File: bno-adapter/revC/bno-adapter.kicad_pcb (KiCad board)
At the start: 2 copper layers, 50.8 x 38.1 mm, 15 parts, among them P1 Mezzanine-Header, P2 CONN_01X04, P3 CONN_01X06, P4 Spacer, P5 Spacer, P6 Spacer, P7 Spacer

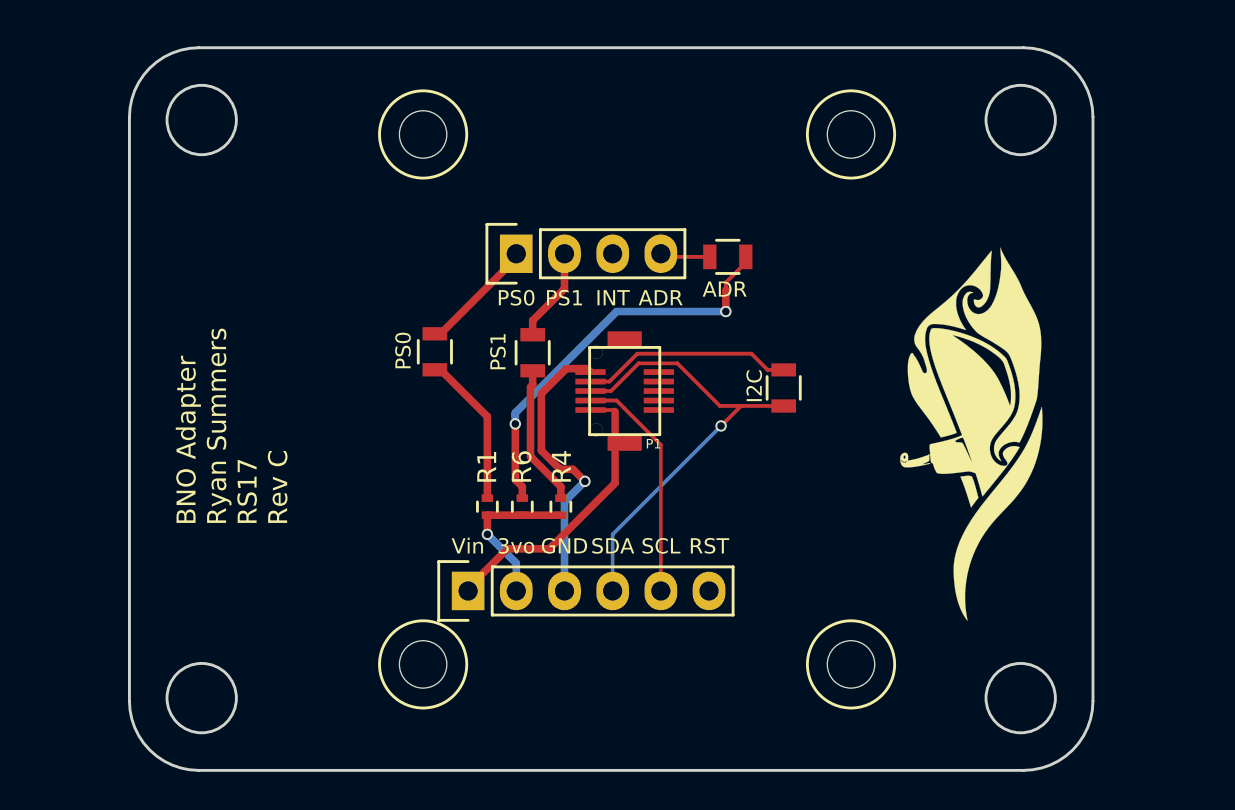
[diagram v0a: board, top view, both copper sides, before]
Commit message: Addition of VRML v2 model files and finished BNO adapter
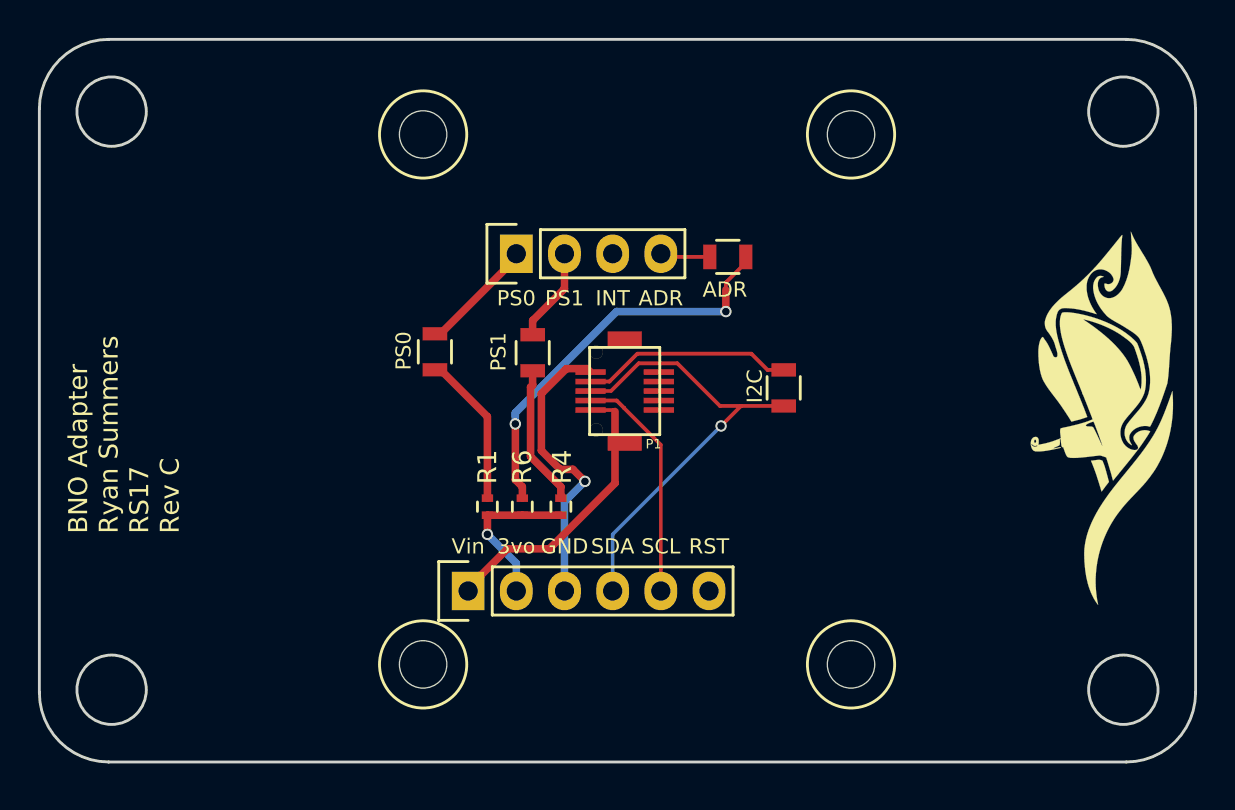
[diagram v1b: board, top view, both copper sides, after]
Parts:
- moved G*** 6.93 mm to (155.4, 101.4)
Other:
- board size 50.8 x 38.1 mm -> 61 x 38.1 mm
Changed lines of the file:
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@@
 (kicad_pcb (version 4) (host pcbnew 4.0.5-e0-6337~49~ubuntu16.04.1)
   (general
-    (links 0)
+    (links 15)
     (no_connects 0)
-    (area 103.785599 81.901203 154.735601 120.151205)
+    (area 99.035799 81.458999 160.145801 119.709001)
     (thickness 1.6)
     (drawings 35)
@@
   )
   (module robosub_footprints:robosub_logo-large (layer F.Cu)
-    (at 148.4884 102.2096 90)
+    (at 155.3718 101.3714 90)
     (fp_text reference G*** (at 0 0 90) (layer F.SilkS) hide
       (effects (font (thickness 0.3)))
@@
       (xy -2.376168 -0.816) (xy -2.374012 -0.812192)) (layer F.SilkS) (width 0.01))
   )
-  (gr_circle (center 107.6706 116.266204) (end 109.4994 116.266204) (layer Edge.Cuts) (width 0.15))
-  (gr_arc (start 107.5182 85.633804) (end 107.5182 81.976204) (angle -90) (layer Edge.Cuts) (width 0.15))
-  (gr_arc (start 151.003 116.418604) (end 151.003 120.076204) (angle -89.9) (layer Edge.Cuts) (width 0.15))
-  (gr_arc (start 107.5182 116.418604) (end 103.8606 116.418604) (angle -90) (layer Edge.Cuts) (width 0.15))
-  (gr_line (start 154.6606 116.418604) (end 154.6606 85.633804) (layer Edge.Cuts) (width 0.15))
-  (gr_circle (center 150.8506 116.266204) (end 152.6794 116.266204) (layer Edge.Cuts) (width 0.15))
-  (gr_line (start 107.5182 120.076204) (end 151.003 120.076204) (layer Edge.Cuts) (width 0.15))
-  (gr_line (start 151.003 81.976204) (end 107.5182 81.976204) (layer Edge.Cuts) (width 0.15))
-  (gr_circle (center 107.6706 85.786204) (end 109.4994 85.786204) (layer Edge.Cuts) (width 0.15))
-  (gr_arc (start 151.003 85.633804) (end 154.6606 85.633804) (angle -90) (layer Edge.Cuts) (width 0.15))
-  (gr_circle (center 150.8506 85.786204) (end 152.6794 85.786204) (layer Edge.Cuts) (width 0.15))
-  (gr_line (start 103.8606 85.633804) (end 103.8606 116.418604) (layer Edge.Cuts) (width 0.15))
-  (gr_text "BNO Adapter\nRyan Summers\nRS17\nRev C" (at 109.2962 107.1626 90) (layer F.SilkS)
+  (gr_line (start 99.1108 85.1916) (end 99.1108 115.9764) (layer Edge.Cuts) (width 0.15))
+  (gr_circle (center 102.9208 115.824) (end 104.7496 115.824) (layer Edge.Cuts) (width 0.15))
+  (gr_circle (center 156.2608 115.824) (end 158.0896 115.824) (layer Edge.Cuts) (width 0.15))
+  (gr_arc (start 102.7684 115.9764) (end 99.1108 115.9764) (angle -90) (layer Edge.Cuts) (width 0.15))
+  (gr_arc (start 156.4132 115.9764) (end 156.4132 119.634) (angle -89.9) (layer Edge.Cuts) (width 0.15))
+  (gr_arc (start 156.4132 85.1916) (end 160.0708 85.1916) (angle -90) (layer Edge.Cuts) (width 0.15))
+  (gr_arc (start 102.7684 85.1916) (end 102.7684 81.534) (angle -90) (layer Edge.Cuts) (width 0.15))
+  (gr_line (start 102.7684 119.634) (end 156.4132 119.634) (layer Edge.Cuts) (width 0.15))
+  (gr_line (start 160.0708 115.9764) (end 160.0708 85.1916) (layer Edge.Cuts) (width 0.15))
+  (gr_line (start 156.4132 81.534) (end 102.7684 81.534) (layer Edge.Cuts) (width 0.15))
+  (gr_circle (center 102.9208 85.344) (end 104.7496 85.344) (layer Edge.Cuts) (width 0.15))
+  (gr_circle (center 156.2608 85.344) (end 158.0896 85.344) (layer Edge.Cuts) (width 0.15))
+  (gr_text "BNO Adapter\nRyan Summers\nRS17\nRev C" (at 103.5812 107.5944 90) (layer F.SilkS)
     (effects (font (size 1 1) (thickness 0.2)) (justify left))
   )

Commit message: converted edge-cut mounting holes to KiCAD components
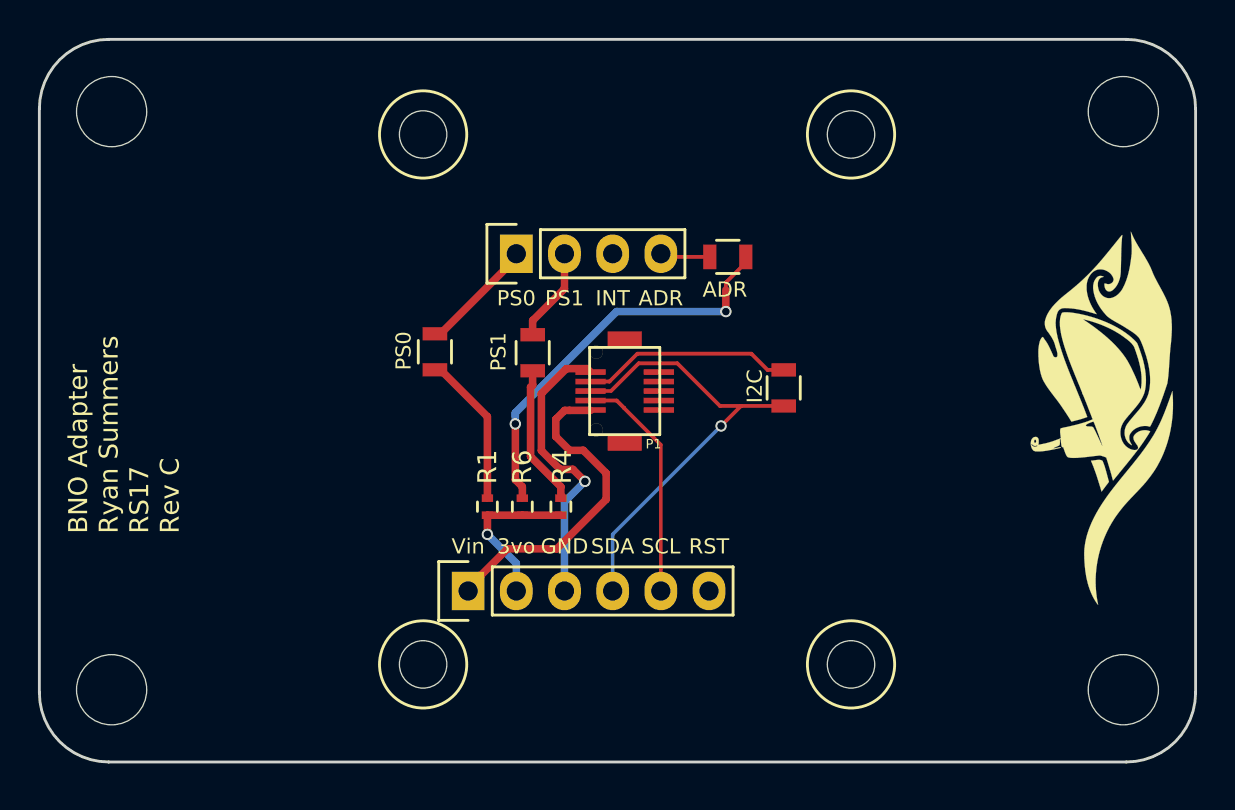
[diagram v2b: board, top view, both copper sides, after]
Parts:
- added REF**: MountingHole_3.7mm, Mounting_Holes:MountingHole_3.7mm, F.Cu at (156.3, 115.8)
- added REF**: MountingHole_3.7mm, Mounting_Holes:MountingHole_3.7mm, F.Cu at (156.3, 85.3)
- added REF**: MountingHole_3.7mm, Mounting_Holes:MountingHole_3.7mm, F.Cu at (102.9, 115.8)
- added REF**: MountingHole_3.7mm, Mounting_Holes:MountingHole_3.7mm, F.Cu at (102.9, 85.3)
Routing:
- net /Vbus: track 15.3 -> 17.1 mm
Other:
- outline, holes or cut-outs redrawn
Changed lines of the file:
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@@
 (kicad_pcb (version 4) (host pcbnew 4.0.5-e0-6337~49~ubuntu16.04.1)
   (general
-    (links 15)
+    (links 0)
     (no_connects 0)
     (area 99.035799 81.458999 160.145801 119.709001)
     (thickness 1.6)
-    (drawings 35)
-    (tracks 75)
+    (drawings 31)
+    (tracks 79)
     (zones 0)
-    (modules 15)
+    (modules 19)
     (nets 13)
   )
@@
     (add_net "Net-(R3-Pad1)")
     (add_net "Net-(R5-Pad1)")
+  )
+  (module Mounting_Holes:MountingHole_3.7mm (layer F.Cu)
+    (at 156.2608 115.824)
+    (descr "Mounting Hole 3.7mm, no annular")
+    (tags "mounting hole 3.7mm no annular")
+    (fp_text reference REF** (at 0 -4.7) (layer F.SilkS) hide
+      (effects (font (size 1 1) (thickness 0.15)))
+    )
+    (fp_text value MountingHole_3.7mm (at 0 4.7) (layer F.Fab)
+      (effects (font (size 1 1) (thickness 0.15)))
+    )
+    (fp_circle (center 0 0) (end 3.7 0) (layer Cmts.User) (width 0.15))
+    (fp_circle (center 0 0) (end 3.95 0) (layer F.CrtYd) (width 0.05))
+    (pad 1 np_thru_hole circle (at 0 0) (size 3.7 3.7) (drill 3.7) (layers *.Cu *.Mask))
+  )
+  (module Mounting_Holes:MountingHole_3.7mm (layer F.Cu)
+    (at 156.2608 85.344)
+    (descr "Mounting Hole 3.7mm, no annular")
+    (tags "mounting hole 3.7mm no annular")
+    (fp_text reference REF** (at 0 -4.7) (layer F.SilkS) hide
+      (effects (font (size 1 1) (thickness 0.15)))
+    )
+    (fp_text value MountingHole_3.7mm (at 0 4.7) (layer F.Fab)
+      (effects (font (size 1 1) (thickness 0.15)))
+    )
+    (fp_circle (center 0 0) (end 3.7 0) (layer Cmts.User) (width 0.15))
+    (fp_circle (center 0 0) (end 3.95 0) (layer F.CrtYd) (width 0.05))
+    (pad 1 np_thru_hole circle (at 0 0) (size 3.7 3.7) (drill 3.7) (layers *.Cu *.Mask))
+  )
+  (module Mounting_Holes:MountingHole_3.7mm (layer F.Cu)
+    (at 102.9208 115.824)
+    (descr "Mounting Hole 3.7mm, no annular")
+    (tags "mounting hole 3.7mm no annular")
+    (fp_text reference REF** (at 0 -4.7) (layer F.SilkS) hide
+      (effects (font (size 1 1) (thickness 0.15)))
+    )
+    (fp_text value MountingHole_3.7mm (at 0 4.7) (layer F.Fab)
+      (effects (font (size 1 1) (thickness 0.15)))
+    )
+    (fp_circle (center 0 0) (end 3.7 0) (layer Cmts.User) (width 0.15))
+    (fp_circle (center 0 0) (end 3.95 0) (layer F.CrtYd) (width 0.05))
+    (pad 1 np_thru_hole circle (at 0 0) (size 3.7 3.7) (drill 3.7) (layers *.Cu *.Mask))
   )
   (module Pin_Headers:Pin_Header_Straight_1x04 (layer F.Cu)
@@
       (xy -2.376168 -0.816) (xy -2.374012 -0.812192)) (layer F.SilkS) (width 0.01))
   )
+  (module Mounting_Holes:MountingHole_3.7mm (layer F.Cu)
+    (at 102.9208 85.344)
+    (descr "Mounting Hole 3.7mm, no annular")
+    (tags "mounting hole 3.7mm no annular")
+    (fp_text reference REF** (at 0 -4.7) (layer F.SilkS) hide
+      (effects (font (size 1 1) (thickness 0.15)))
+    )
+    (fp_text value MountingHole_3.7mm (at 0 4.7) (layer F.Fab)
+      (effects (font (size 1 1) (thickness 0.15)))
+    )
+    (fp_circle (center 0 0) (end 3.7 0) (layer Cmts.User) (width 0.15))
+    (fp_circle (center 0 0) (end 3.95 0) (layer F.CrtYd) (width 0.05))
+    (pad 1 np_thru_hole circle (at 0 0) (size 3.7 3.7) (drill 3.7) (layers *.Cu *.Mask))
+  )
   (gr_line (start 99.1108 85.1916) (end 99.1108 115.9764) (layer Edge.Cuts) (width 0.15))
-  (gr_circle (center 102.9208 115.824) (end 104.7496 115.824) (layer Edge.Cuts) (width 0.15))
-  (gr_circle (center 156.2608 115.824) (end 158.0896 115.824) (layer Edge.Cuts) (width 0.15))
   (gr_arc (start 102.7684 115.9764) (end 99.1108 115.9764) (angle -90) (layer Edge.Cuts) (width 0.15))
   (gr_arc (start 156.4132 115.9764) (end 156.4132 119.634) (angle -89.9) (layer Edge.Cuts) (width 0.15))
@@
   (gr_line (start 160.0708 115.9764) (end 160.0708 85.1916) (layer Edge.Cuts) (width 0.15))
   (gr_line (start 156.4132 81.534) (end 102.7684 81.534) (layer Edge.Cuts) (width 0.15))
-  (gr_circle (center 102.9208 85.344) (end 104.7496 85.344) (layer Edge.Cuts) (width 0.15))
-  (gr_circle (center 156.2608 85.344) (end 158.0896 85.344) (layer Edge.Cuts) (width 0.15))
   (gr_text "BNO Adapter\nRyan Summers\nRS17\nRev C" (at 103.5812 107.5944 90) (layer F.SilkS)
     (effects (font (size 1 1) (thickness 0.2)) (justify left))
@@
   (segment (start 131.8768 109.411) (end 131.8768 110.617) (width 0.19) (layer F.Cu) (net 2))
   (segment (start 131.8768 102.910876) (end 131.8768 109.411) (width 0.19) (layer F.Cu) (net 2))
-  (segment (start 128.1718 101.076) (end 129.3843 101.076) (width 0.2) (layer F.Cu) (net 3))
-  (segment (start 129.3843 101.076) (end 129.4638 101.1555) (width 0.2) (layer F.Cu) (net 3))
-  (segment (start 129.4163 101.1555) (end 129.4638 101.1555) (width 0.19) (layer F.Cu) (net 3))
-  (segment (start 129.4638 104.930502) (end 129.4638 101.1555) (width 0.4) (layer F.Cu) (net 3))
-  (segment (start 123.7869 108.3945) (end 125.999802 108.3945) (width 0.4) (layer F.Cu) (net 3))
-  (segment (start 125.999802 108.3945) (end 129.4638 104.930502) (width 0.4) (layer F.Cu) (net 3))
   (segment (start 121.7168 110.617) (end 121.7168 110.4646) (width 0.4) (layer F.Cu) (net 3))
+  (segment (start 128.9939 104.4067) (end 127.7874 103.2002) (width 0.4) (layer F.Cu) (net 3))
   (segment (start 121.7168 110.4646) (end 123.7869 108.3945) (width 0.4) (layer F.Cu) (net 3))
+  (segment (start 126.3396 102.4763) (end 126.3396 101.5619) (width 0.4) (layer F.Cu) (net 3))
+  (segment (start 123.7869 108.3945) (end 126.3904 108.3945) (width 0.4) (layer F.Cu) (net 3))
+  (segment (start 127.7874 103.2002) (end 127.0635 103.2002) (width 0.4) (layer F.Cu) (net 3))
+  (segment (start 126.3396 101.5619) (end 126.805499 101.096001) (width 0.4) (layer F.Cu) (net 3))
+  (segment (start 126.3904 108.3945) (end 128.9939 105.791) (width 0.4) (layer F.Cu) (net 3))
+  (segment (start 128.9939 105.791) (end 128.9939 104.4067) (width 0.4) (layer F.Cu) (net 3))
+  (segment (start 127.0635 103.2002) (end 126.3396 102.4763) (width 0.4) (layer F.Cu) (net 3))
+  (segment (start 126.805499 101.096001) (end 127.075799 101.096001) (width 0.4) (layer F.Cu) (net 3))
+  (segment (start 127.075799 101.096001) (end 128.1718 101.096001) (width 0.4) (layer F.Cu) (net 3))
   (segment (start 136.6504 98.1075) (end 130.6403 98.1075) (width 0.2) (layer F.Cu) (net 4))
   (segment (start 129.1718 99.576) (end 128.1718 99.576) (width 0.2) (layer F.Cu) (net 4))
